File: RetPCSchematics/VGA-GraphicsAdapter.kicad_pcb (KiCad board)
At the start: 2 copper layers, 136.7 x 101.3 mm, 51 parts, among them J1 Bus_ISA_8bit, J2 74320-9004, J3 Conn_01x03_Male, U1 74AUC2G125, U10 ATmega644P-20PU, U11 IS61LV5128AL-10TLI, U12 74LS245, U13 SN74LVC245AN, U15 74LVC2G240, U16 74LVC2G240, U17 74LVC1G18, U18 74LVC1G18, U19 74LVC1G18, U2 74LVC2G240, U20 74LVC1G18, U21 ATF22V10D, U22 74LS245A, U23 74LVC1G373, U24 74LVC1G373, U25 74LVC1G373, U26 74LVC1G373, U27 74LVC1G373, U28 74LVC1G373, U29 74LVC1G373, U3 ATF22V10D, U30 74LVC1G373, U31 74LVC1G373, U32 74LVC1G373, U33 74LVC1G373, U34 74LVC1G373, U36 TFP410, U37 ATF750C, U4 ATF22V10D, U5 74LS245, U6 ATF22V10D, U7 74LS245A, U8 74LS245, U9 74LS245A, X1 DGOF5S3

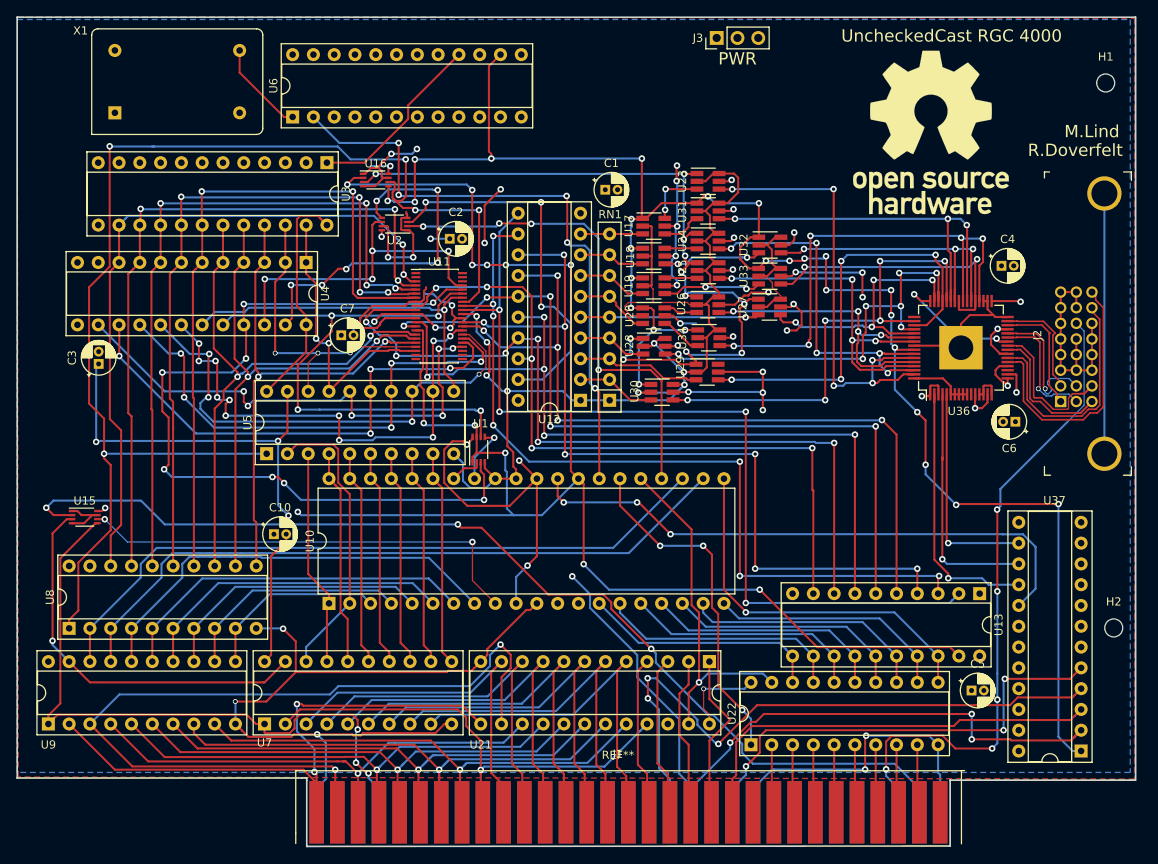
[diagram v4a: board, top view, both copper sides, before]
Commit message: Upgraded to Rev 4.0C
CPLD minimal smd components rework of Rev 4.0
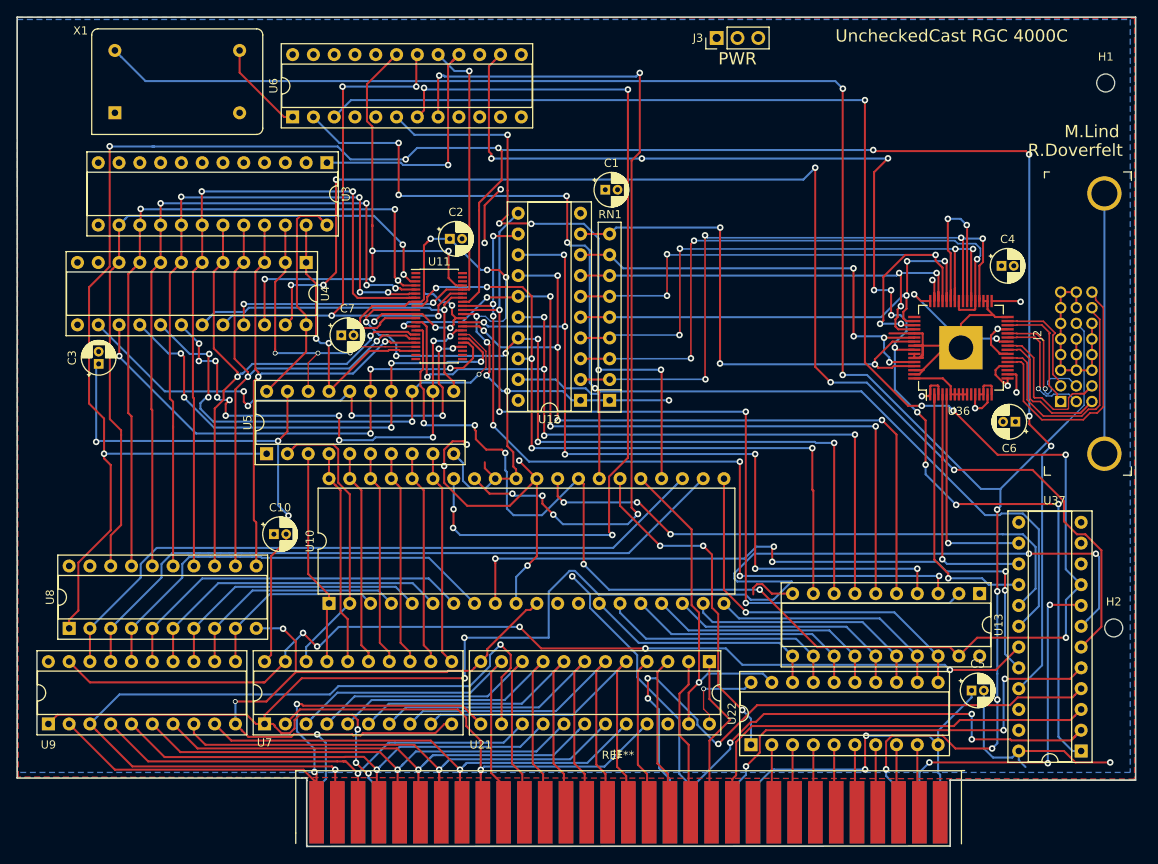
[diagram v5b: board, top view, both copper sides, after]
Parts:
- removed REF**: OSHW-Logo_19x20mm_SilkScreen, Symbol:OSHW-Logo_19x20mm_SilkScreen
- removed U1: 74AUC2G125, Package_SO:VSSOP-8_2.3x2mm_P0.5mm
- removed U15, U16, U2: 74LVC2G240, Package_SO:VSSOP-8_2.3x2mm_P0.5mm
- removed U17, U18, U19, U20: 74LVC1G18, Package_TO_SOT_SMD:SOT-23-6_Handsoldering
- removed U23, U24, U25, U26, U27, U28, U29, U30, U31, U32, U33, U34: 74LVC1G373, Package_TO_SOT_SMD:SOT-23-6_Handsoldering
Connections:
- J1 pad 12: (no net) -> Net-(J1-Pad12)
- J1 pad 15: (no net) -> Net-(J1-Pad15)
- J1 pad 16: (no net) -> Net-(J1-Pad16)
- J1 pad 17: (no net) -> Net-(J1-Pad17)
- J1 pad 18: (no net) -> Net-(J1-Pad18)
- J1 pad 19: (no net) -> Net-(J1-Pad19)
- J1 pad 20: (no net) -> Net-(J1-Pad20)
- J1 pad 21: (no net) -> Net-(J1-Pad21)
- J1 pad 22: (no net) -> Net-(J1-Pad22)
- J1 pad 23: (no net) -> Net-(J1-Pad23)
- J1 pad 24: (no net) -> Net-(J1-Pad24)
- J1 pad 25: (no net) -> Net-(J1-Pad25)
- J1 pad 26: (no net) -> Net-(J1-Pad26)
- J1 pad 27: (no net) -> Net-(J1-Pad27)
- J1 pad 29: (no net) -> Net-(J1-Pad29)
- J1 pad 30: (no net) -> Net-(J1-Pad30)
- J1 pad 32: (no net) -> Net-(J1-Pad32)
- J1 pad 4: (no net) -> Net-(J1-Pad4)
- J1 pad 41: (no net) -> Net-(J1-Pad41)
- J1 pad 5: (no net) -> Net-(J1-Pad5)
- J1 pad 6: (no net) -> Net-(J1-Pad6)
- J1 pad 7: (no net) -> Net-(J1-Pad7)
- J1 pad 8: (no net) -> Net-(J1-Pad8)
- J1 pad 9: (no net) -> Net-(J1-Pad9)
- U10 pad 12: (no net) -> Net-(U10-Pad12)
- U10 pad 13: (no net) -> Net-(U10-Pad13)
- U11 pad 1: (no net) -> Net-(U11-Pad1)
- U11 pad 2: (no net) -> Net-(U11-Pad2)
- U11 pad 21: (no net) -> Net-(U11-Pad21)
- U11 pad 22: (no net) -> Net-(U11-Pad22)
- U11 pad 23: (no net) -> Net-(U11-Pad23)
- U11 pad 24: (no net) -> Net-(U11-Pad24)
- U11 pad 25: (no net) -> Net-(U11-Pad25)
- U11 pad 42: (no net) -> Net-(U11-Pad42)
- U11 pad 43: (no net) -> Net-(U11-Pad43)
- U11 pad 44: (no net) -> Net-(U11-Pad44)
- U21 pad 22: (no net) -> Net-(U21-Pad22)
- U3 pad 10: (no net) -> Net-(U3-Pad10)
- U3 pad 11: (no net) -> Net-(U3-Pad11)
- U3 pad 13: (no net) -> Net-(U3-Pad13)
- U3 pad 2: (no net) -> Net-(U3-Pad2)
- U3 pad 3: (no net) -> Net-(U3-Pad3)
- U3 pad 4: (no net) -> Net-(U3-Pad4)
- U3 pad 5: (no net) -> Net-(U3-Pad5)
- U3 pad 6: (no net) -> Net-(U3-Pad6)
- U3 pad 7: (no net) -> Net-(U3-Pad7)
- U3 pad 8: (no net) -> Net-(U3-Pad8)
- U3 pad 9: (no net) -> Net-(U3-Pad9)
- U36 pad 11: (no net) -> Net-(U36-Pad11)
- U36 pad 19: (no net) -> Net-(U36-Pad19)
- U36 pad 36: Net-(U34-Pad4) -> Net-(RN1-Pad2)
- U36 pad 37: Net-(U33-Pad4) -> Net-(RN1-Pad3)
- U36 pad 38: Net-(U32-Pad4) -> Net-(RN1-Pad4)
- U36 pad 39: Net-(U31-Pad4) -> GND
- U36 pad 40: Net-(U34-Pad4) -> Net-(RN1-Pad2)
- U36 pad 41: Net-(U33-Pad4) -> Net-(RN1-Pad3)
- U36 pad 42: Net-(U32-Pad4) -> Net-(RN1-Pad4)
- U36 pad 43: Net-(U31-Pad4) -> GND
- U36 pad 44: Net-(U30-Pad4) -> Net-(RN1-Pad5)
- U36 pad 45: Net-(U29-Pad4) -> Net-(RN1-Pad6)
- U36 pad 46: Net-(U28-Pad4) -> Net-(RN1-Pad7)
- U36 pad 47: Net-(U27-Pad4) -> GND
- U36 pad 49: (no net) -> Net-(U36-Pad49)
- U36 pad 50: Net-(U30-Pad4) -> Net-(RN1-Pad5)
- U36 pad 51: Net-(U29-Pad4) -> Net-(RN1-Pad6)
- U36 pad 52: Net-(U28-Pad4) -> Net-(RN1-Pad7)
- U36 pad 53: Net-(U27-Pad4) -> GND
- U36 pad 54: Net-(U26-Pad4) -> Net-(RN1-Pad8)
- U36 pad 55: Net-(U25-Pad4) -> Net-(RN1-Pad9)
- U36 pad 58: Net-(U24-Pad4) -> GND
- U36 pad 59: Net-(U23-Pad4) -> GND
- U36 pad 60: Net-(U26-Pad4) -> Net-(RN1-Pad8)
- U36 pad 61: Net-(U25-Pad4) -> Net-(RN1-Pad9)
- U36 pad 62: Net-(U24-Pad4) -> GND
- U36 pad 63: Net-(U23-Pad4) -> GND
- U37 pad 10: (no net) -> Net-(U37-Pad10)
- U37 pad 11: (no net) -> Net-(U37-Pad11)
- U37 pad 13: (no net) -> Net-(U37-Pad13)
- U37 pad 18: (no net) -> GEnd(inv)
- U37 pad 19: (no net) -> ALEN(inv)
- U37 pad 20: (no net) -> RST(inv)
- U37 pad 21: (no net) -> (inv)LE
- U37 pad 22: (no net) -> Net-(U37-Pad22)
- U37 pad 23: (no net) -> Net-(U37-Pad23)
- U37 pad 6: (no net) -> GEnd
- U37 pad 7: (no net) -> ALEN
- U37 pad 8: (no net) -> RST
- U37 pad 9: (no net) -> LoadEnable
- U4 pad 11: (no net) -> Net-(U4-Pad11)
- U4 pad 13: (no net) -> Net-(U4-Pad13)
- U6 pad 10: (no net) -> Net-(U6-Pad10)
- U6 pad 11: (no net) -> Net-(U6-Pad11)
- U6 pad 13: (no net) -> Net-(U6-Pad13)
- U6 pad 15: (no net) -> Net-(U6-Pad15)
- U6 pad 17: (no net) -> /VA17
- U6 pad 18: (no net) -> /VA16
- U6 pad 19: (no net) -> /VA18
- U6 pad 20: (no net) -> Net-(U6-Pad20)
- U6 pad 21: (no net) -> Net-(U6-Pad21)
- U6 pad 22: (no net) -> Net-(U6-Pad22)
- U6 pad 23: (no net) -> Net-(U6-Pad23)
- U6 pad 3: (no net) -> LoadEnable
- U6 pad 4: (no net) -> Net-(U6-Pad4)
- U6 pad 5: (no net) -> Net-(U6-Pad5)
- U6 pad 6: (no net) -> /XA18
- U6 pad 7: (no net) -> /XA16
- U6 pad 8: (no net) -> /XA17
- U6 pad 9: (no net) -> Net-(U6-Pad9)
- X1 pad 1: (no net) -> Net-(X1-Pad1)
- X1 pad 14: +3V3 -> +FEMV
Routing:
- net +FEMV: track 80.3 -> 231.2 mm, vias 5 -> 7
- net (inv)LE: track 153.1 -> 286.7 mm, vias 5 -> 8
- net GEnd: track 43.6 -> 164.6 mm
- net ALEN: track 86.8 -> 203.5 mm, vias 3 -> 7
- net /XA16: track 4.01 -> 110.3 mm, vias 0 -> 5
- net Net-(U16-Pad3): track 101.4 -> 0.00 mm, vias 11 -> 0
- net /XA17: track 7.20 -> 107.9 mm, vias 1 -> 6
- net RST: track 129.8 -> 44.4 mm
- net ALEN(inv): track 69.6 -> 146.9 mm, vias 1 -> 5
- net Net-(RN1-Pad2): track 9.64 -> 83.3 mm, vias 0 -> 4
- net LoadEnable: track 198.2 -> 268.8 mm, vias 12 -> 10
- net Net-(RN1-Pad4): track 8.46 -> 74.1 mm, vias 0 -> 4
- net +3V3: track 237.2 -> 171.6 mm, vias 41 -> 17
- net GND: track 486.7 -> 423.5 mm, vias 24 -> 22
- net Net-(RN1-Pad6): track 9.14 -> 72.2 mm, vias 0 -> 5
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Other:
- board text added: "UncheckedCast RGC 4000C"
- board text removed: "UncheckedCast RGC 4000"

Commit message: some unpushed changes?
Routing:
- net LoadEnable: track 268.8 -> 267.8 mm
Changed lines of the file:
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@@
-(kicad_pcb (version 20171130) (host pcbnew "(5.0.0)")
+(kicad_pcb (version 20171130) (host pcbnew 5.0.2+dfsg1-1)
   (general
     (thickness 1.6)
     (drawings 17)
-    (tracks 2070)
+    (tracks 2067)
     (zones 0)
     (modules 30)
@@
   (segment (start 180.213 102.743) (end 179.578 102.108) (width 0.25) (layer F.Cu) (net 43) (status 30))
   (segment (start 180.213 112.5474) (end 180.213 102.743) (width 0.25) (layer F.Cu) (net 43) (status 20))
-  (segment (start 166.915 96.146891) (end 166.915 95.581206) (width 0.25) (layer F.Cu) (net 43))
-  (segment (start 167.03601 96.267901) (end 166.915 96.146891) (width 0.25) (layer F.Cu) (net 43))
-  (segment (start 167.03601 97.28761) (end 167.03601 96.267901) (width 0.25) (layer F.Cu) (net 43))
-  (segment (start 168.306801 98.558401) (end 167.03601 97.28761) (width 0.25) (layer F.Cu) (net 43))
-  (segment (start 170.237201 98.558401) (end 168.306801 98.558401) (width 0.25) (layer F.Cu) (net 43))
   (segment (start 170.6372 98.9584) (end 170.237201 98.558401) (width 0.25) (layer F.Cu) (net 43))
   (via (at 239.141 121.539) (size 0.8) (drill 0.4) (layers F.Cu B.Cu) (net 43))
@@
   (segment (start 151.7904 55.8546) (end 149.733 57.912) (width 0.25) (layer B.Cu) (net 43))
   (segment (start 214.5792 55.8546) (end 151.7904 55.8546) (width 0.25) (layer B.Cu) (net 43))
+  (segment (start 169.892195 98.558401) (end 166.915 95.581206) (width 0.25) (layer F.Cu) (net 43))
+  (segment (start 170.237201 98.558401) (end 169.892195 98.558401) (width 0.25) (layer F.Cu) (net 43))
   (segment (start 197.358 102.108) (end 197.358 115.682998) (width 0.25) (layer F.Cu) (net 44) (status 10))
   (segment (start 223.52 127) (end 223.52 123.7742) (width 0.25) (layer F.Cu) (net 44) (status 30))
